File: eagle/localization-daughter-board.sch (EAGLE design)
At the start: 22 parts, among them U1 LM340MP-5.0/NOPB, U2 RPI-ZERO, U3 LMS8117AMP-ADJ/NOPB, U4 TXS0101DCKR, U5 SN65HVD256DR, U6 STM32F042FXP

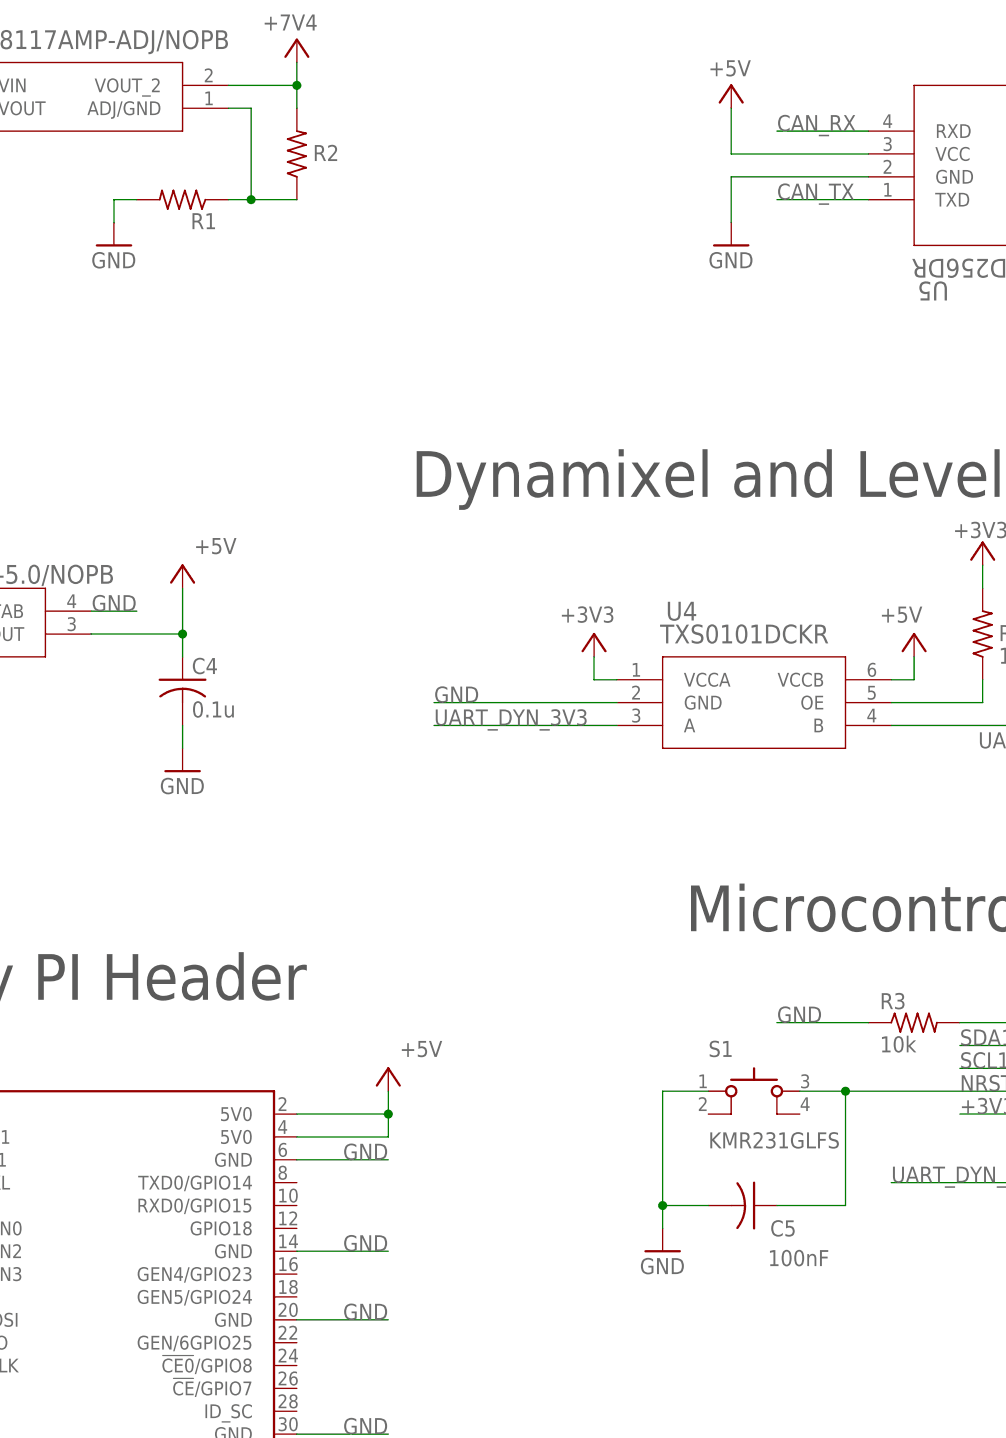
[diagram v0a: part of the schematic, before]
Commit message: Updated schematic and BOM
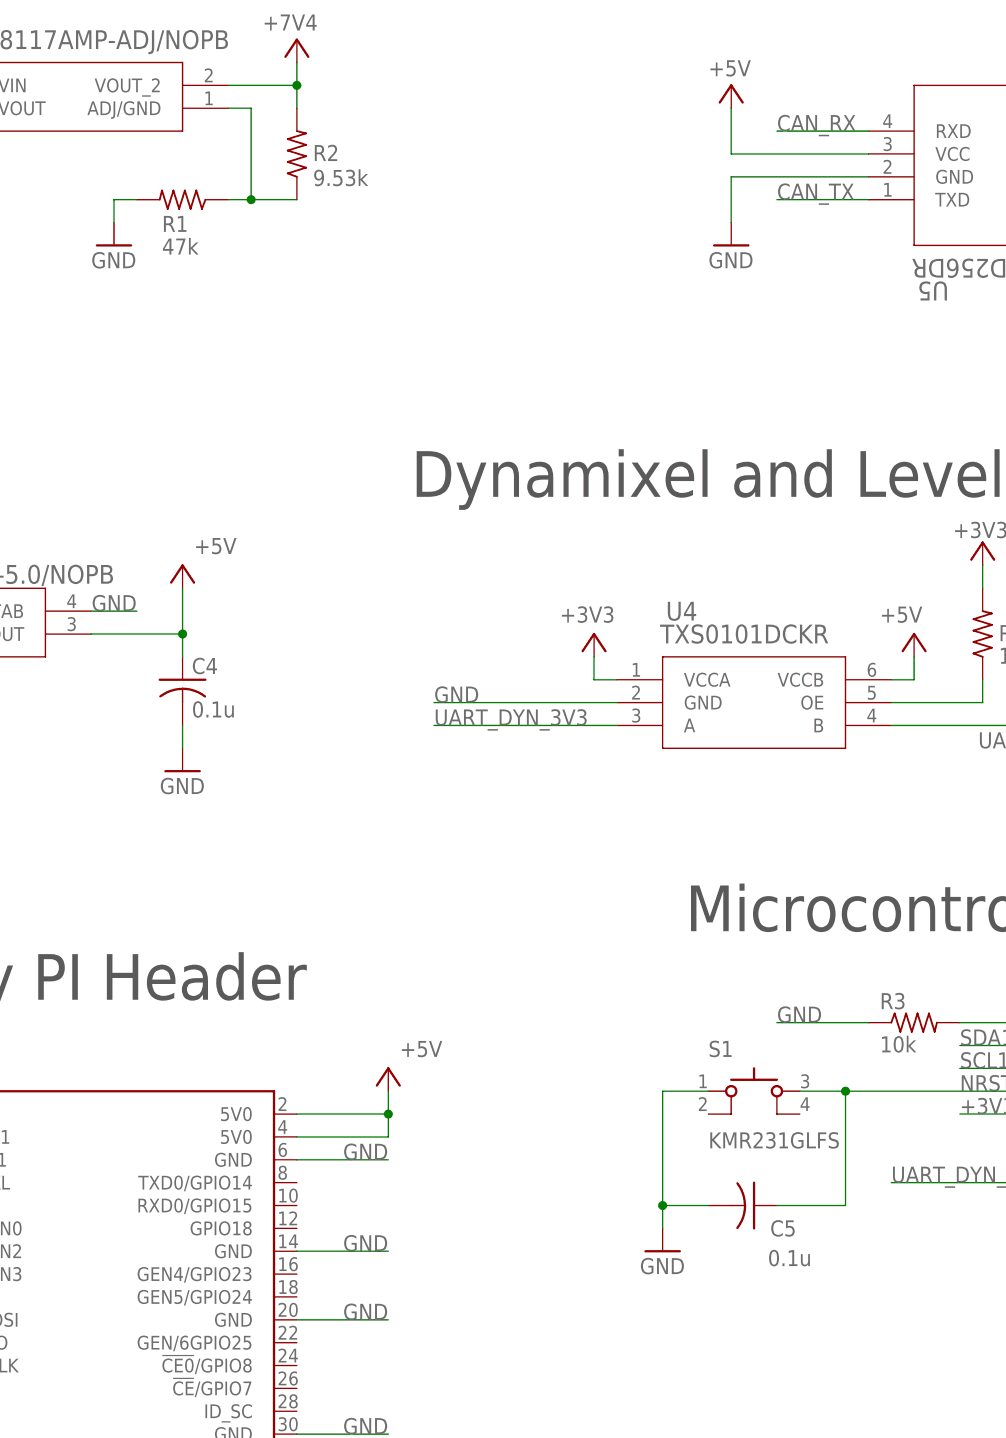
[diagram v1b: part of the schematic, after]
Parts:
- C5: value 100nF -> 0.1u
- R1: value (none) -> 47k
- R2: value (none) -> 9.53k

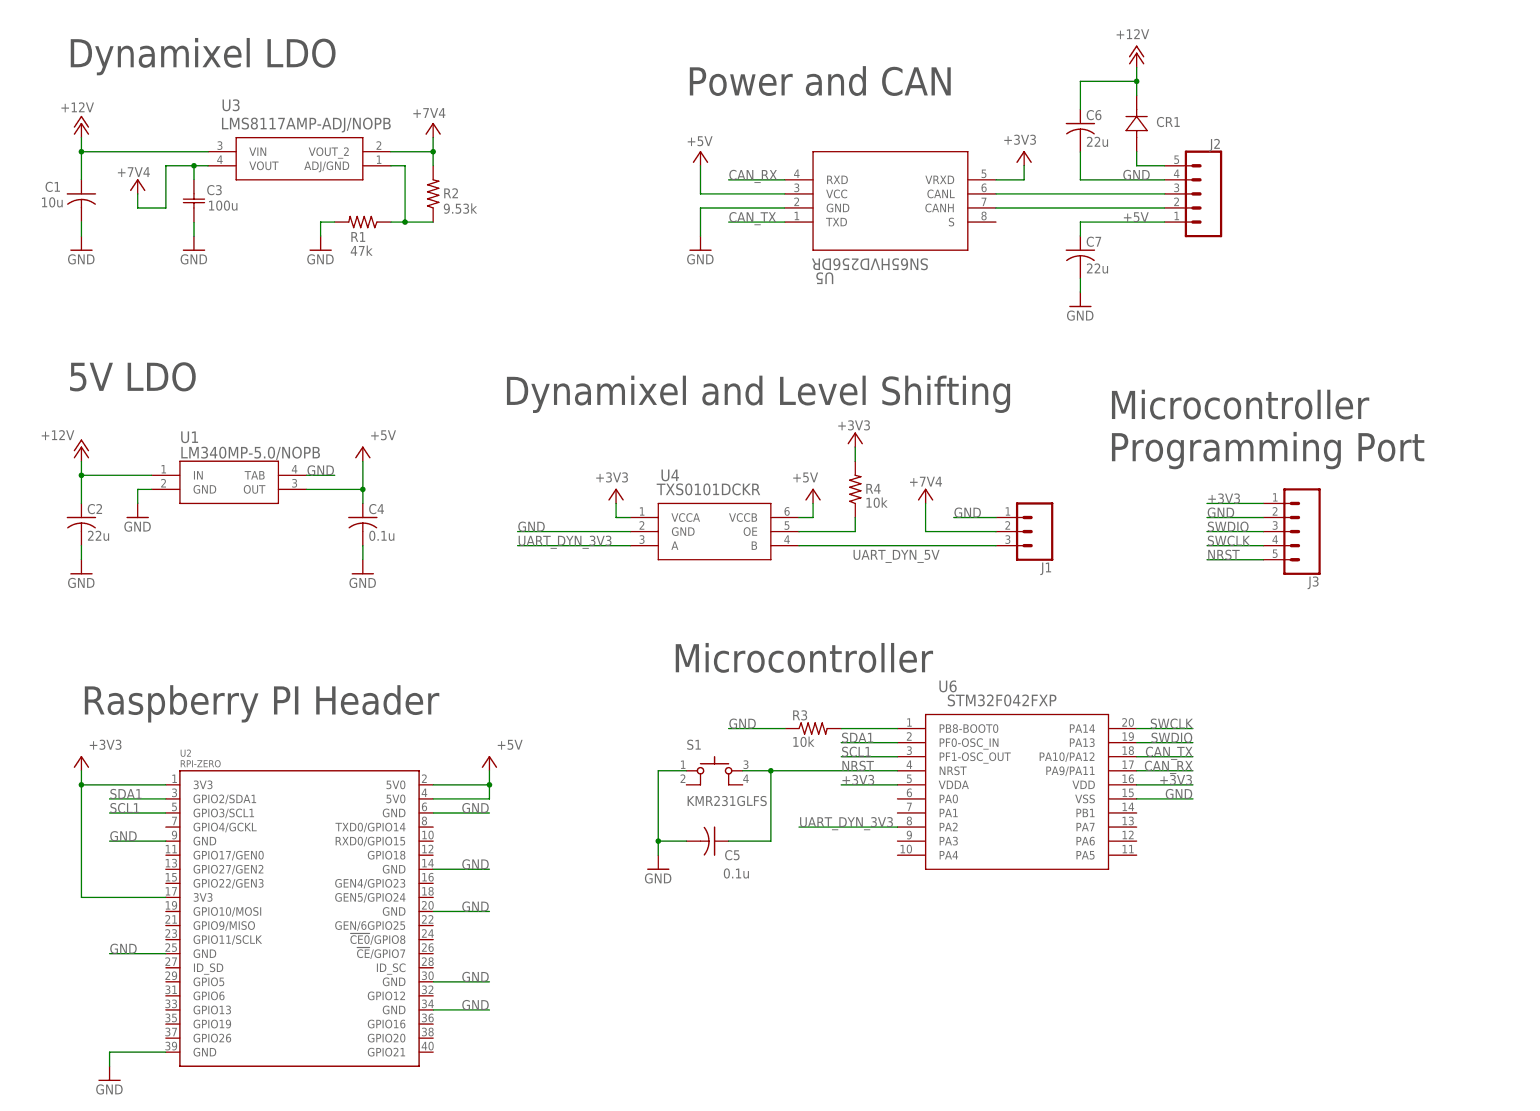
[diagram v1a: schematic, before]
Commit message: Added most of the new components
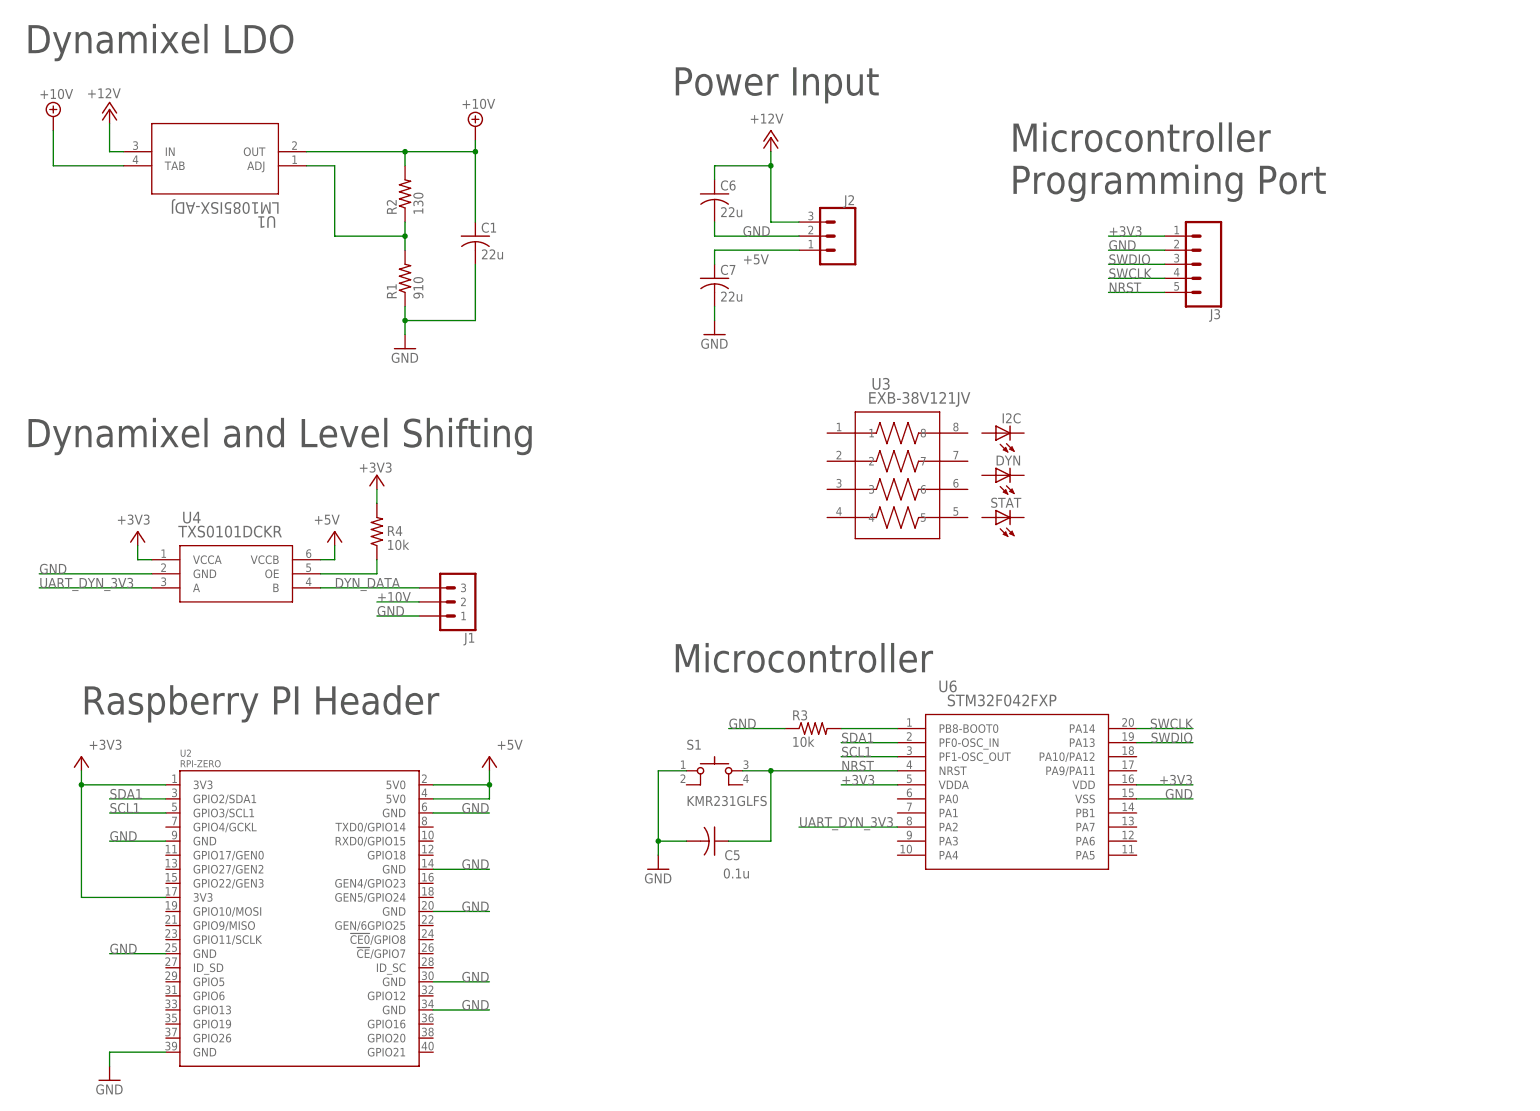
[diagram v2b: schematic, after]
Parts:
- removed C2: 22u, resistor:C-USC0805
- removed C3: 100u, Localization-Daughter-Board:F931C107MCC
- removed C4: 0.1u, resistor:C-USC0805
- removed CR1: STPS2H100A, Localization-Daughter-Board:STPS2H100A
- removed U5: SN65HVD256DR, Localization-Daughter-Board:SN65HVD256DR
- added DYN, I2C, STAT: (no value), led:LEDSML0603
- C1: value 10u -> 22u
- J1: value (none) -> MOLEX-22-03-5035; device Localization-Daughter-Board:CONN_03 -> bbb_localization_cape:MOLEX-22-03-5035
- J2: device SparkFun-Connectors:CONN_05JST-VERT -> SparkFun-Connectors:CONN_03JST-PTH
- J3: device SparkFun-Connectors:CONN_05 -> SparkFun-Connectors:CONN_05JST
- R1: value 47k -> 910
- R2: value 9.53k -> 130
- U1: value LM340MP-5.0/NOPB -> LM1085ISX-ADJ; device Localization-Daughter-Board:LM340MP-5.0/NOPB -> bbb_localization_cape:LM1085ISX-ADJ
- U3: value LMS8117AMP-ADJ/NOPB -> EXB-38V121JV; device Localization-Daughter-Board:LMS8117AMP-ADJ/NOPB -> Localization-Daughter-Board:EXB-38V121JV
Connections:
- net UART_DYN_5V renamed DYN_DATA
- removed net +7V4: C3.1, J1.2, R2.2, U3.VOUT, U3.VOUT_2
- removed net CAN_RX: U5.RXD, U6.PA9/PA11
- removed net CAN_TX: U5.TXD, U6.PA10/PA12
- removed net N$2: J2.2, U5.CANH
- removed net N$4: R1.1, R2.1, U3.ADJ/GND
- removed net VIN: CR1.22, J2.5
- new net +10V: C1.1, J1.2, R2.2, U1.OUT, U1.TAB
- net +12V: now also J2.3; no longer C1.1, C2.1, CR1.11, U3.VIN
- net +3V3: no longer U5.VRXD
- net +5V: no longer C4.1, U1.OUT, U5.VCC
- net GND: now also J2.2, R1.1; no longer C2.2, C3.2, C4.2, J2.4, R1.2, U1.GND, U1.TAB, U5.GND
- net N$3: now also R1.2, R2.1, U1.ADJ; no longer J2.3, U5.CANL
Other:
- note added: "Power Input"
- note removed: "5V LDO"
- note removed: "Power and CAN"
- moved on the sheet: C1, C6, C7, J3, R1, R2, R4, U1, U4

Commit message: Finished layout, need to do final check
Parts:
- removed STAT: (no value), led:LEDSML0603
- added SJ1: (no value), jumper:SJ
- added STAT1, STAT2: (no value), led:LEDSML0603
- J3: device SparkFun-Connectors:CONN_05JST -> SparkFun-Connectors:CONN_05JST-VERT
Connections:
- new net DYN_LED: U3.3, U6.PA1
- new net I2C_LED: U3.4, U6.PA0
- new net N$2: STAT1.A, U3.7
- new net N$4: DYN.A, U3.6
- new net N$5: I2C.A, U3.5
- new net N$6: STAT2.A, U3.8
- new net PI_NRST: SJ1.2, U2.GPIO17/GEN0
- new net PI_RX: U2.RXD0/GPIO15, U6.PA9/PA11
- new net PI_TX: U2.TXD0/GPIO14, U6.PA10/PA12
- new net STAT_LED: U3.1, U6.PA4
- new net TRACK_LED: U3.2, U6.PA3
- net GND: now also DYN.C, I2C.C, STAT1.C, STAT2.C
- net NRST: now also SJ1.1
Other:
- moved on the sheet: DYN, I2C, R3

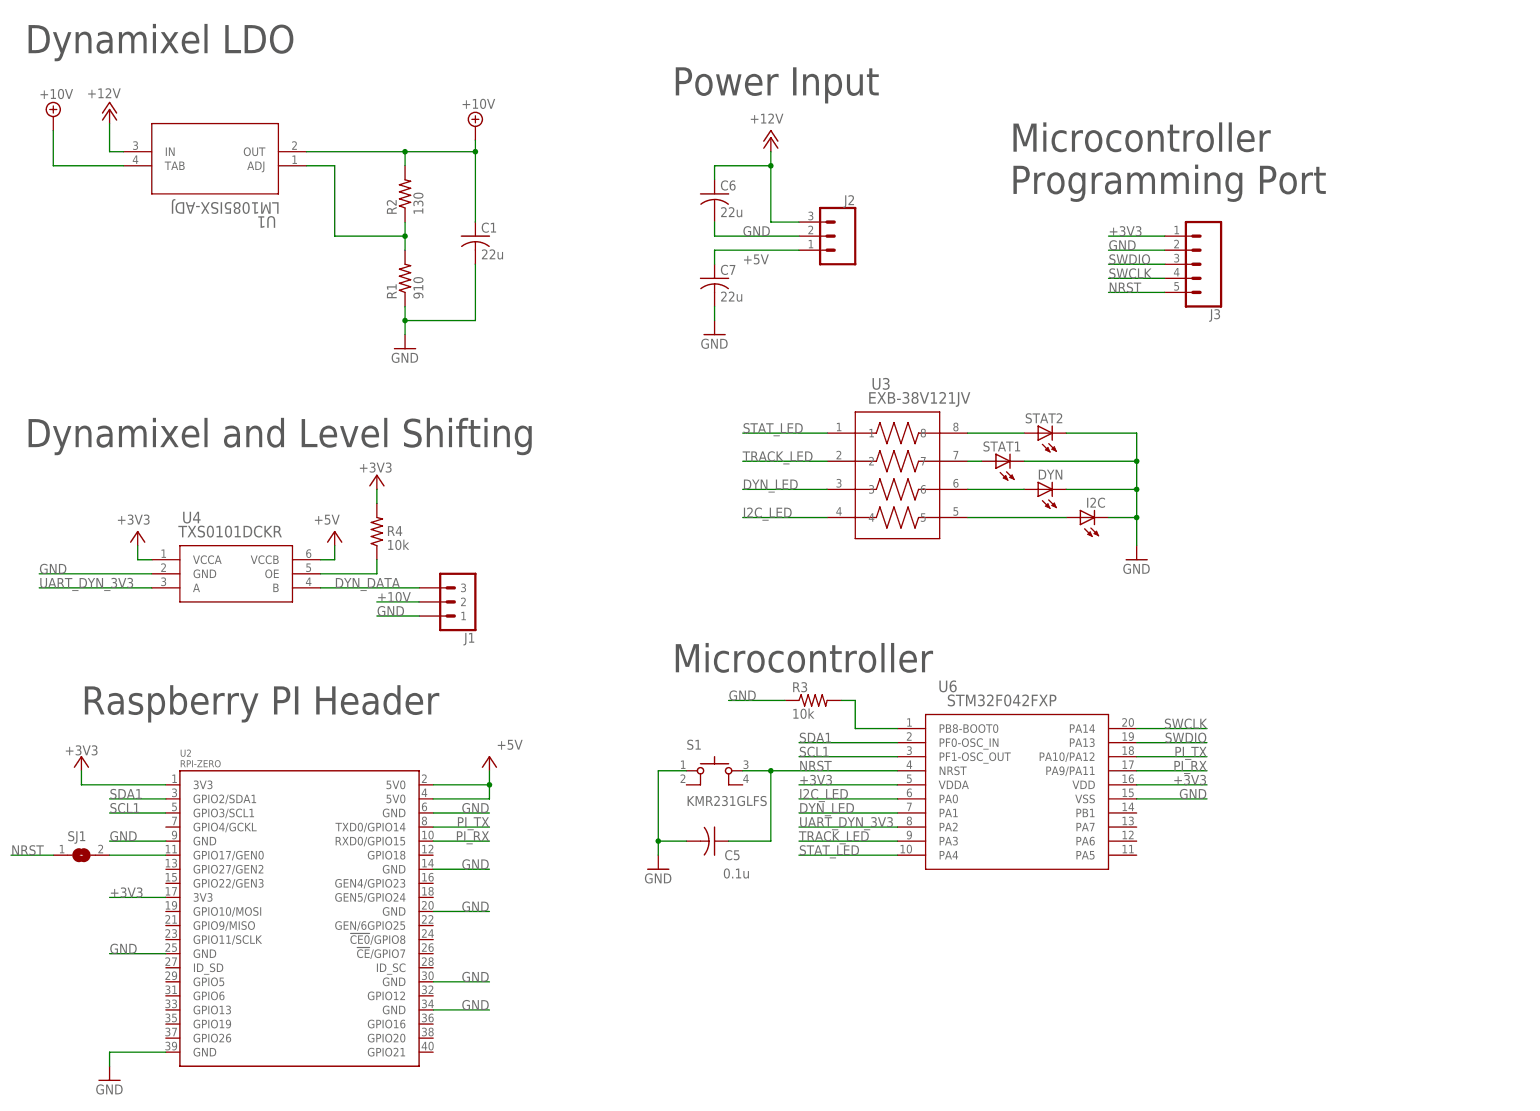
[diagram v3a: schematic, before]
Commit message: Added a few comments to the schematic
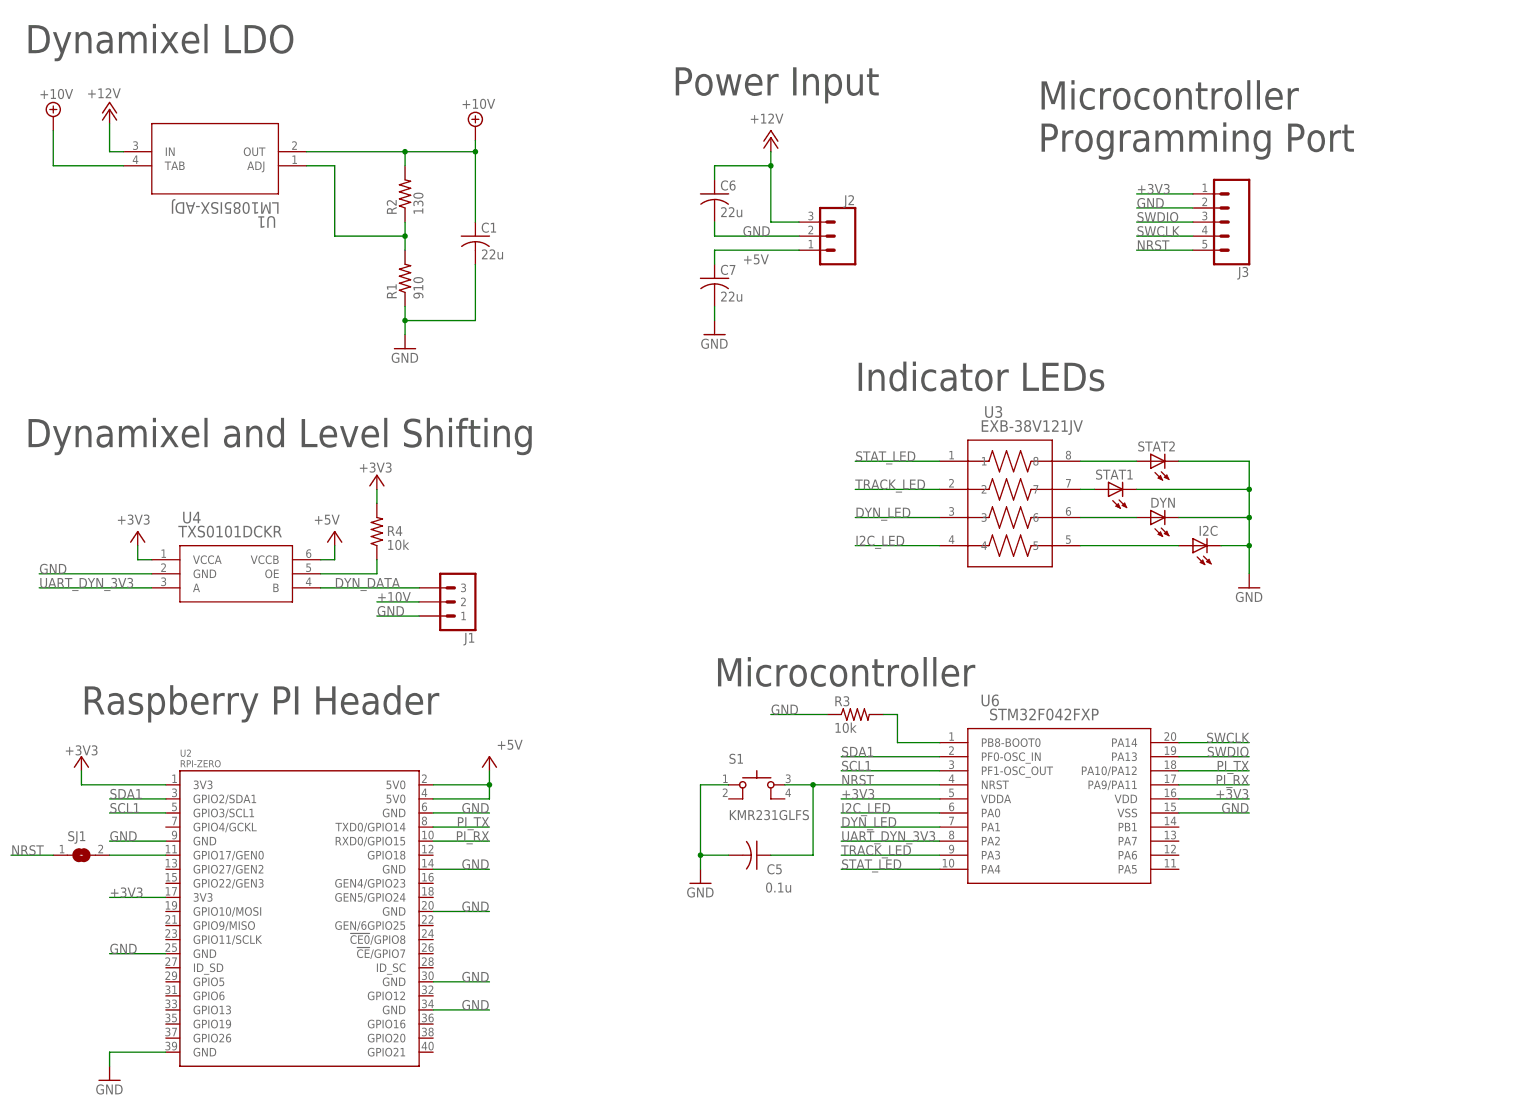
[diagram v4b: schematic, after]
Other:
- note added: "Indicator LEDs"
- moved on the sheet: C5, DYN, I2C, J3, R3, S1, STAT1, STAT2, U3, U6
